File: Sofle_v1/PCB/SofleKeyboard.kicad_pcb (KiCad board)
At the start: 2 copper layers, 137.2 x 109.2 mm, 87 parts, among them J1 LED, J2 4PIN, J3 OLED, P1 i2c_pin, P2 i2c_pin, SW1 SW_PUSH, SW10 SW_PUSH, SW11 SW_PUSH, SW12 SW_PUSH, SW13 SW_PUSH, SW14 SW_PUSH, SW15 SW_PUSH, SW16 SW_PUSH, SW17 SW_PUSH, SW18 SW_PUSH, SW19 SW_PUSH, SW2 SW_PUSH, SW20 SW_PUSH, SW21 SW_PUSH, SW22 SW_PUSH, SW23 SW_PUSH, SW24 SW_PUSH, SW25 Rotary_Encoder_Switch, SW26 SW_PUSH, SW27 SW_PUSH, SW28 SW_PUSH, SW29 SW_PUSH, SW3 SW_PUSH, SW30 SW_PUSH, SW4 SW_PUSH, SW5 SW_PUSH, SW6 SW_PUSH, SW7 SW_PUSH, SW8 SW_PUSH, SW9 SW_PUSH, U1 ProMicro

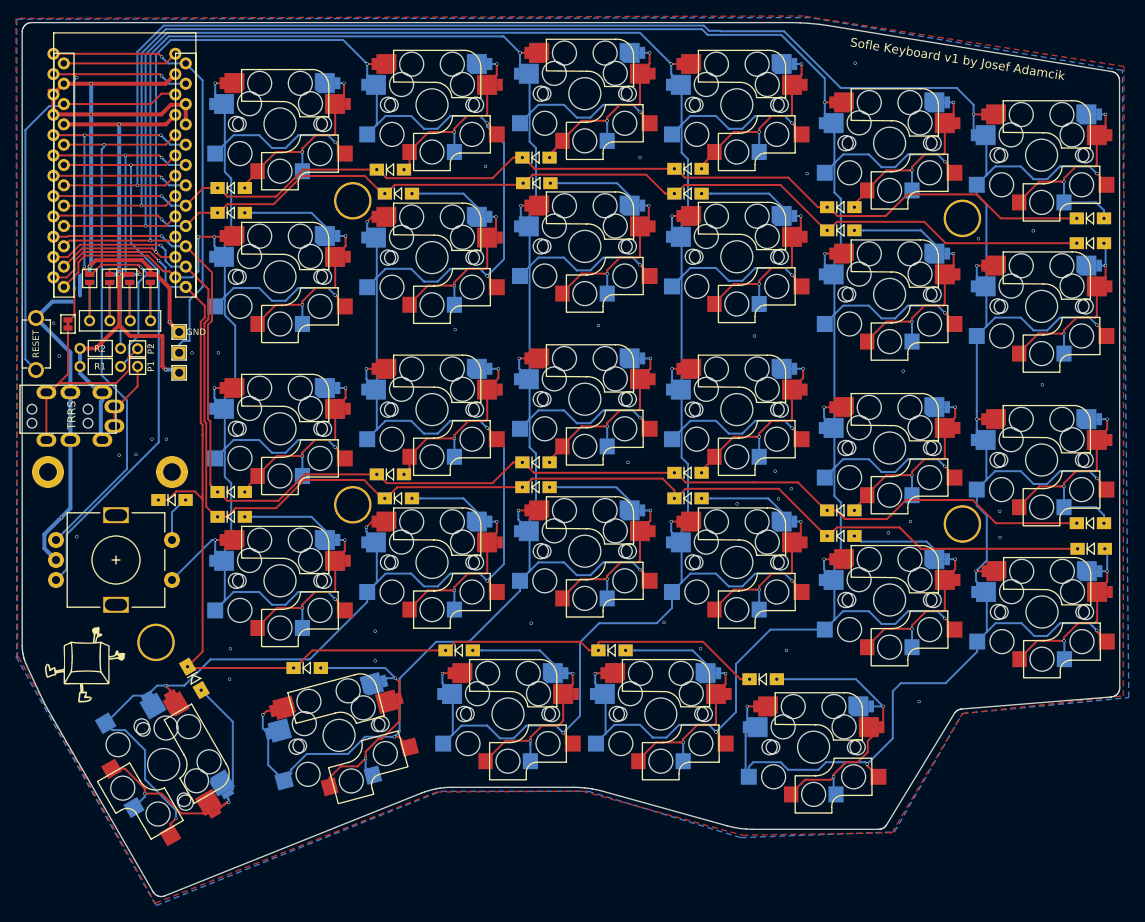
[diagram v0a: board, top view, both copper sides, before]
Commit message: First pass at comparison graphics Revised all keyboards to use outline stubbs Generated nested SVG's and color pallete
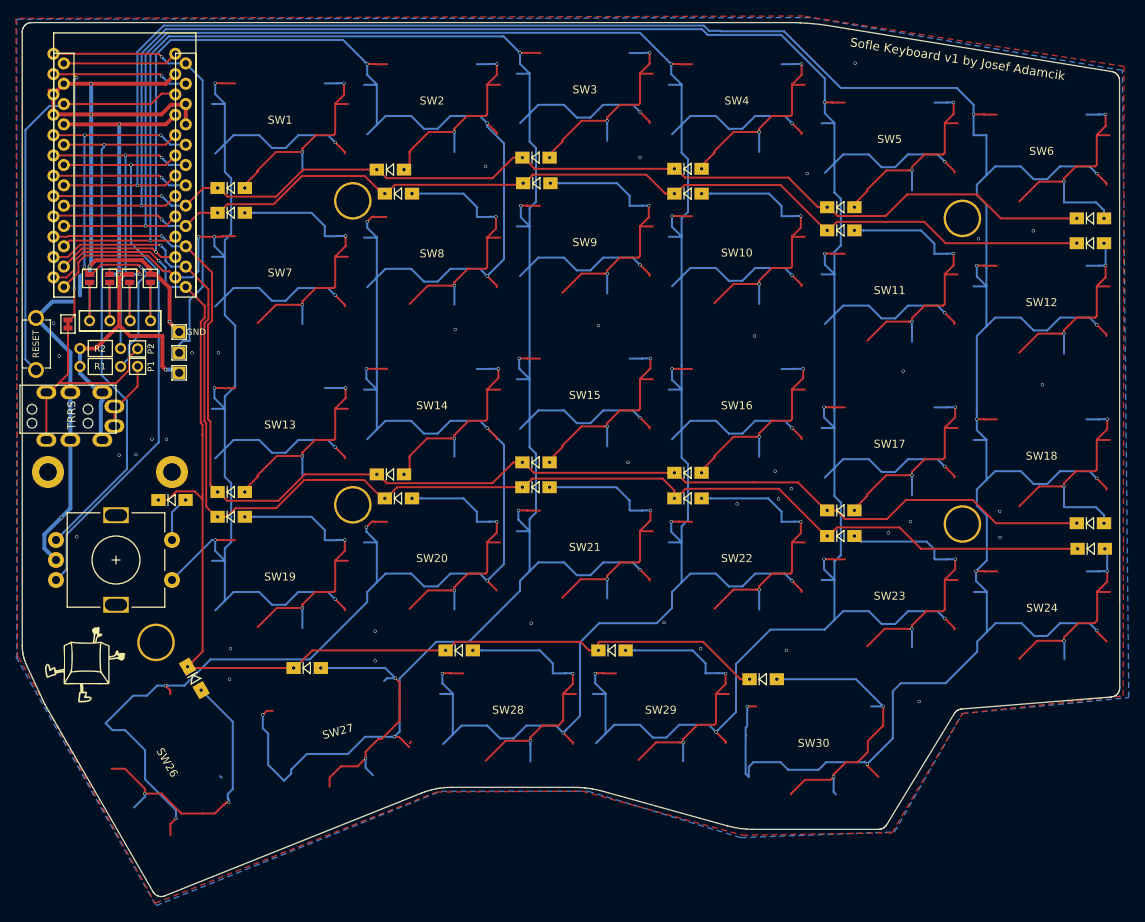
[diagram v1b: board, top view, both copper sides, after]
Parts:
- SW1, SW10, SW11, SW12, SW13, SW14, SW15, SW16, SW17, SW18, SW19, SW2, SW20, SW21, SW22, SW23, SW24, SW27, SW28, SW29, SW3, SW30, SW4, SW5, SW6, SW7, SW8, SW9: footprint SofleKeyboard-footprint:CherryMX_KailhLowProfile_Hotswap -> ergodonk_kicad_library:key_outline_only
- SW26: footprint SofleKeyboard-footprint:CherryMX_KailhLowProfile_Hotswap_1.5 -> ergodonk_kicad_library:key_outline_only
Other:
- net class Default removed
- net class GND removed
- net class VCC removed
